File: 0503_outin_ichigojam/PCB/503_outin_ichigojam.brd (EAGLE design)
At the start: 75 x 50 mm, 25 parts

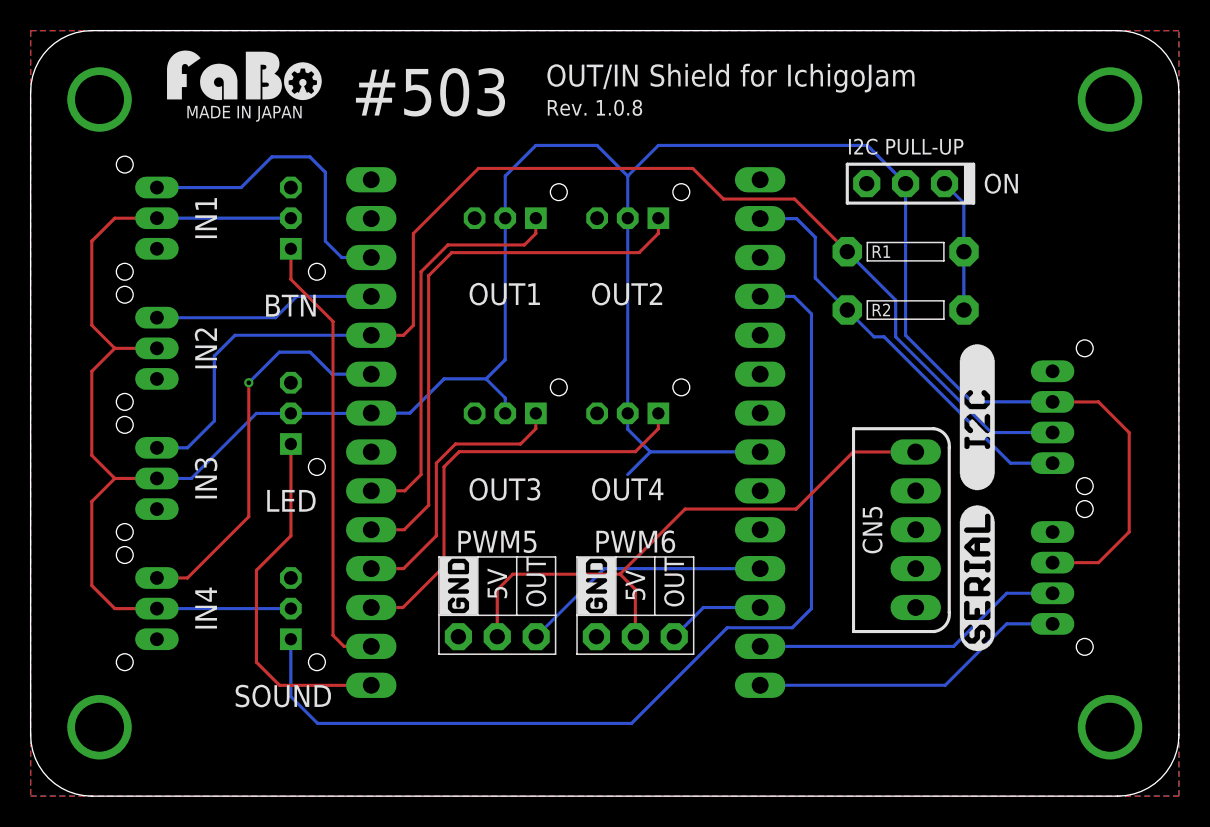
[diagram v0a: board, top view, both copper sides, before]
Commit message: #503 outin_ichigojam　ロゴ修正
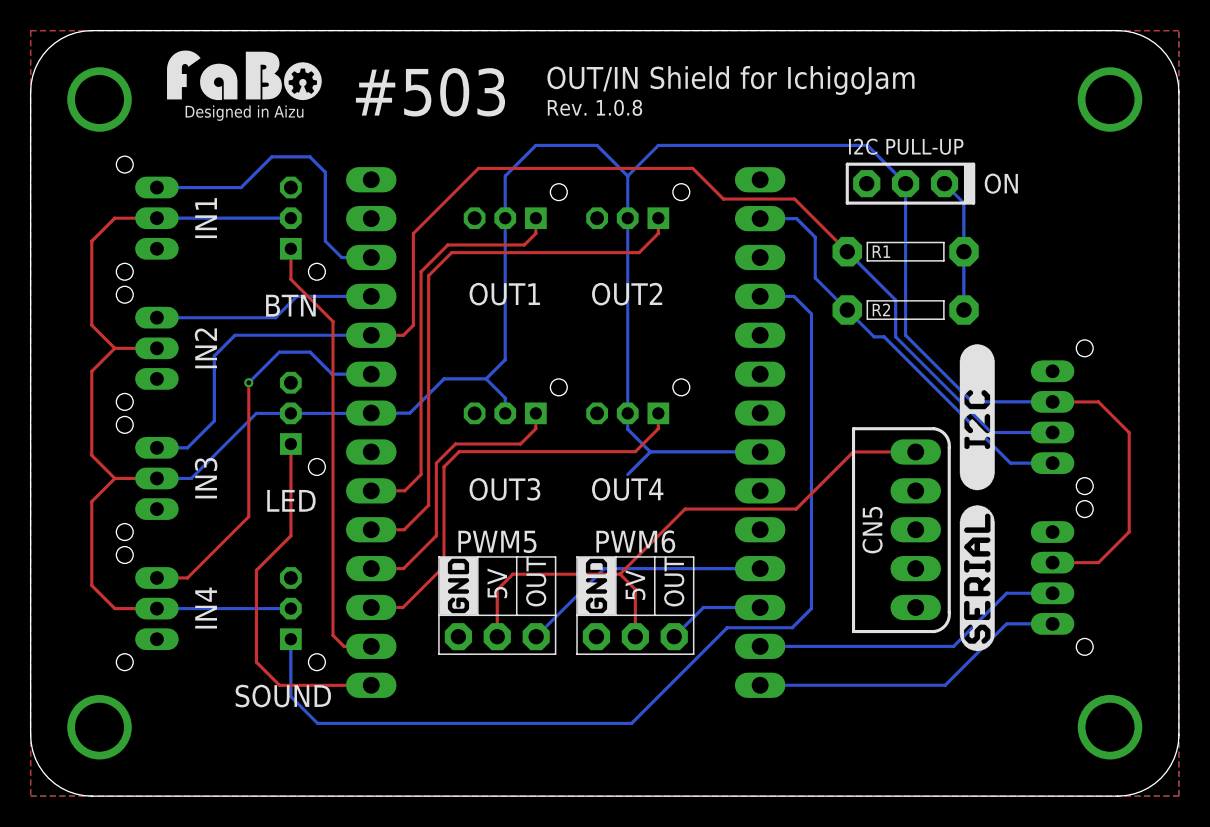
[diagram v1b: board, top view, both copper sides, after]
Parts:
- removed U$3: (no value), FaBo-etc:LOGO_FABO_MS
- added LOGO1: (no value), component:LOGO_FABO_M
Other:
- board text added: "Designed in Aizu"
- board text removed: "MADE IN JAPAN"
